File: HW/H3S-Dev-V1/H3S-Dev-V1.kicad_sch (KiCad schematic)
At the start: 74 parts, among them J1 USB_C_Receptacle_USB2.0_16P, J2 Conn_01x02, J3 Conn_Coaxial, J4 Conn_01x04, J5 Conn_01x04, Q1 DMP3099L, SW1 SW_Push, SW2 SW_Push, U1 Ra-01SH-P, U2 LTC4054ES5-4.2, U3 USBLC6-2SC6, U4 ESP32-S3-WROOM-1, U5 SY8089AAAC, U6 L96-M33

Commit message: Routing progress
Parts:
- added C14: 22u, Capacitor_SMD:C_0805_2012Metric_Pad1.18x1.45mm_HandSolder, symbol Device:C
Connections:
- net GND: now also C14.2
- net VCC: now also C14.1
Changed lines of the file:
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@@
 	(wire
 		(pts
+			(xy 372.11 73.66) (xy 372.11 80.01)
+		)
+		(stroke
+			(width 0)
+			(type default)
+		)
+	)
+	(wire
+		(pts
 			(xy 154.94 185.42) (xy 154.94 189.23)
 		)
@@
 	(wire
 		(pts
+			(xy 372.11 92.71) (xy 372.11 87.63)
+		)
+		(stroke
+			(width 0)
+			(type default)
+		)
+	)
+	(wire
+		(pts
 			(xy 57.15 82.55) (xy 40.64 82.55)
 		)
@@
 	)
 	(symbol
+		(lib_id "power:GND")
+		(at 372.11 92.71 0)
+		(unit 1)
+		(exclude_from_sim no)
+		(in_bom yes)
+		(on_board yes)
+		(dnp no)
+		(fields_autoplaced yes)
+		(property "Reference" "#PWR049"
+			(at 372.11 99.06 0)
+			(effects
+				(font
+					(size 1.27 1.27)
+				)
+				(hide yes)
+			)
+		)
+		(property "Value" "GND"
+			(at 372.11 97.79 0)
+			(effects
+				(font
+					(size 1.27 1.27)
+				)
+			)
+		)
+		(property "Footprint" ""
+			(at 372.11 92.71 0)
+			(effects
+				(font
+					(size 1.27 1.27)
+				)
+				(hide yes)
+			)
+		)
+		(property "Datasheet" ""
+			(at 372.11 92.71 0)
+			(effects
+				(font
+					(size 1.27 1.27)
+				)
+				(hide yes)
+			)
+		)
+		(property "Description" "Power symbol creates a global label with name \"GND\" , ground"
+			(at 372.11 92.71 0)
+			(effects
+				(font
+					(size 1.27 1.27)
+				)
+				(hide yes)
+			)
+		)
+		(pin "1"
+		)
+		(instances
+			(project "H3S-Dev-V1"
+				(path "/bea38324-05bc-47f3-9040-a69798280d79"
+					(reference "#PWR049")
+					(unit 1)
+				)
+			)
+		)
+	)
+	(symbol
 		(lib_id "RF_Module:ESP32-S3-WROOM-1")
 		(at 144.78 139.7 0)
@@
 					(unit 1)
 				)
+			)
+		)
+	)
+	(symbol
+		(lib_id "power:VCC")
+		(at 372.11 73.66 0)
+		(unit 1)
+		(exclude_from_sim no)
+		(in_bom yes)
+		(on_board yes)
+		(dnp no)
+		(fields_autoplaced yes)
+		(property "Reference" "#PWR048"
+			(at 372.11 77.47 0)
+			(effects
+				(font
+					(size 1.27 1.27)
+				)
+				(hide yes)
+			)
+		)
+		(property "Value" "VCC"
+			(at 372.11 68.58 0)
+			(effects
+				(font
+					(size 1.27 1.27)
+				)
+			)
+		)
+		(property "Footprint" ""
+			(at 372.11 73.66 0)
+			(effects
+				(font
+					(size 1.27 1.27)
+				)
+				(hide yes)
+			)
+		)
+		(property "Datasheet" ""
+			(at 372.11 73.66 0)
+			(effects
+				(font
+					(size 1.27 1.27)
+				)
+				(hide yes)
+			)
+		)
+		(property "Description" "Power symbol creates a global label with name \"VCC\""
+			(at 372.11 73.66 0)
+			(effects
+				(font
+					(size 1.27 1.27)
+				)
+				(hide yes)
+			)
+		)
+		(pin "1"
+		)
+		(instances
+			(project "H3S-Dev-V1"
+				(path "/bea38324-05bc-47f3-9040-a69798280d79"
+					(reference "#PWR048")
+					(unit 1)
+				)
+			)
+		)
+	)
+	(symbol
+		(lib_id "Device:C")
+		(at 372.11 83.82 0)
+		(unit 1)
+		(exclude_from_sim no)
+		(in_bom yes)
+		(on_board yes)
+		(dnp no)
+		(property "Reference" "C14"
+			(at 368.554 81.28 0)
+			(effects
+				(font
+					(size 1.27 1.27)
+				)
+				(justify left)
+			)
+		)
+		(property "Value" "22u"
+			(at 368.046 86.106 0)
+			(effects
+				(font
+					(size 1.27 1.27)
+				)
+				(justify left)
+			)
+		)
+		(property "Footprint" "Capacitor_SMD:C_0805_2012Metric_Pad1.18x1.45mm_HandSolder"
+			(at 373.0752 87.63 0)
+			(effects
+				(font
+					(size 1.27 1.27)
+				)
+				(hide yes)
+			)
+		)
+		(property "Datasheet" "~"
+			(at 372.11 83.82 0)
+			(effects
+				(font
+					(size 1.27 1.27)
+				)
+				(hide yes)
+			)
+		)
+		(property "Description" "Unpolarized capacitor"
+			(at 372.11 83.82 0)
+			(effects
+				(font
+					(size 1.27 1.27)
+				)
+				(hide yes)
+			)
+		)
+		(pin "1"
+		)
+		(pin "2"
+		)
+		(instances
+			(project "H3S-Dev-V1"
+				(path "/bea38324-05bc-47f3-9040-a69798280d79"
+					(reference "C14")
+					(unit 1)
+				)

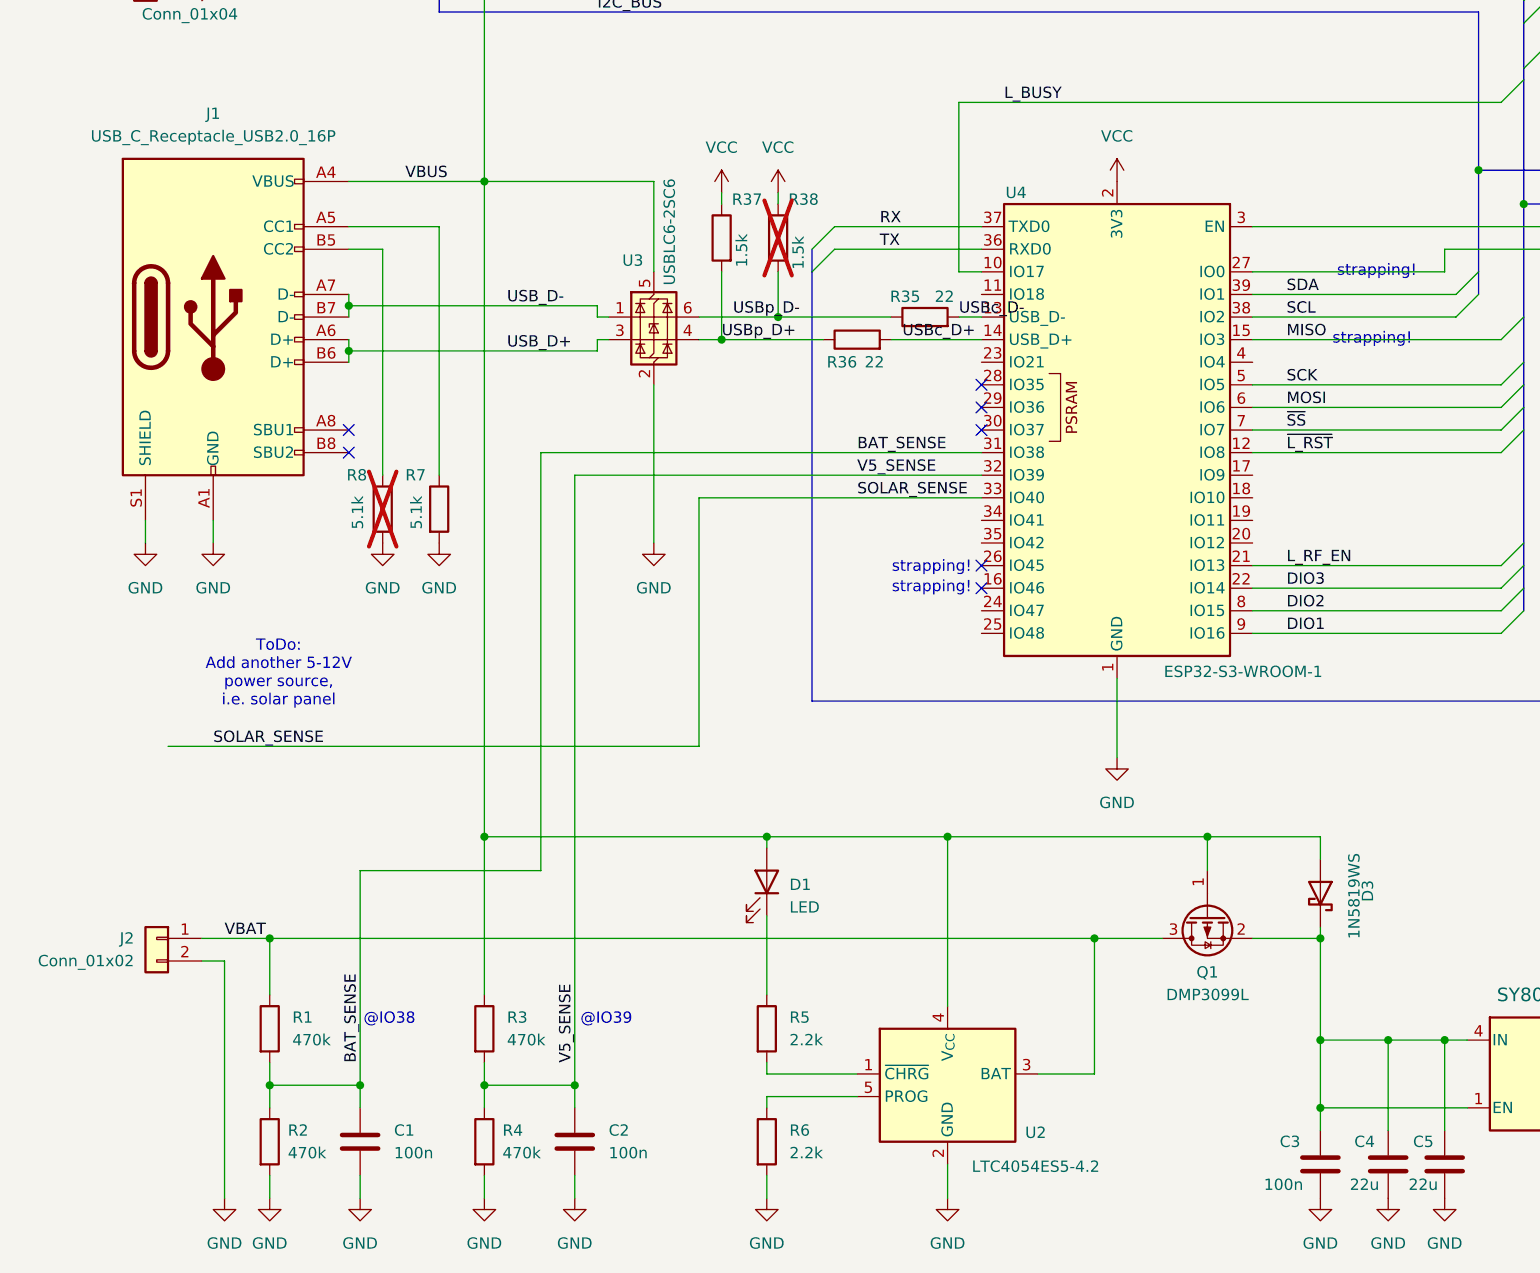
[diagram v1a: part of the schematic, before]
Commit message: Solar connector added
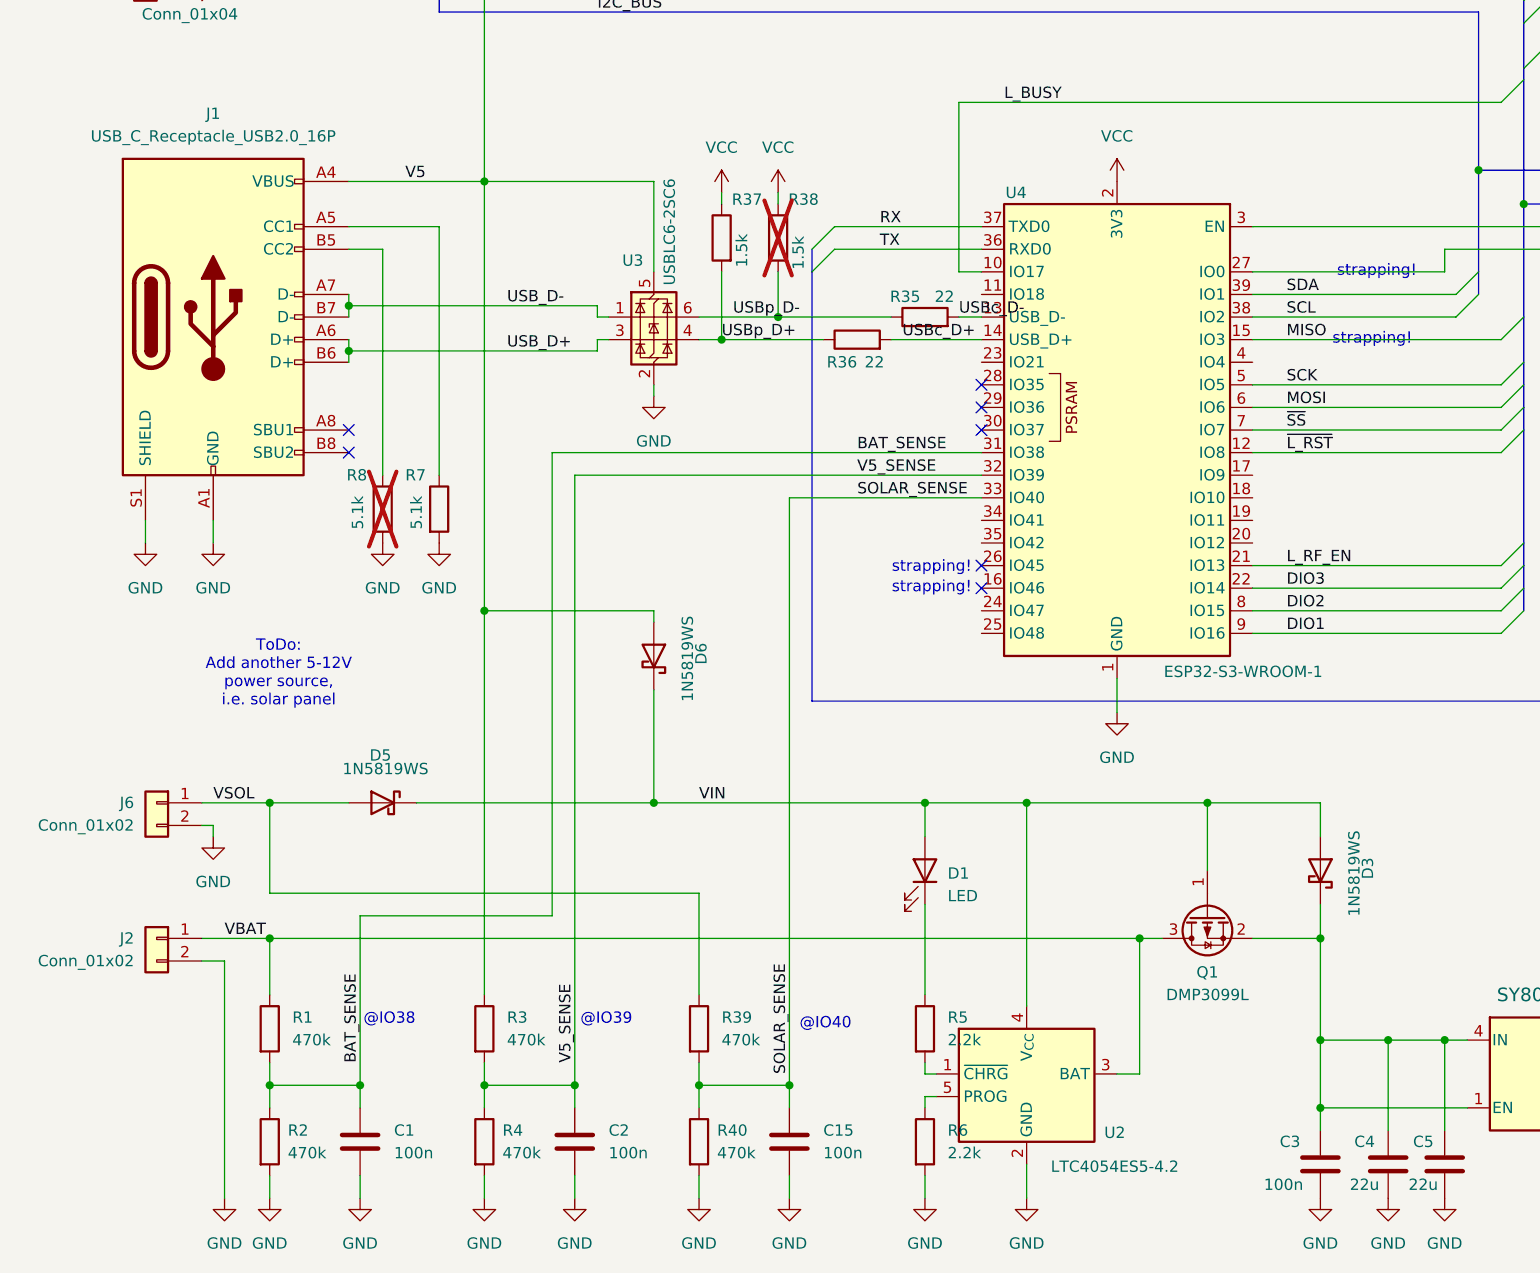
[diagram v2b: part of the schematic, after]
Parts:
- added C15: 100n, Capacitor_SMD:C_0603_1608Metric, symbol Device:C
- added D5, D6: 1N5819WS, Diode_SMD:D_SOD-323, symbol Diode:1N5819WS
- added J6: Conn_01x02, Connector_JST:JST_PH_B2B-PH-K_1x02_P2.00mm_Vertical, symbol Connector_Generic:Conn_01x02
- added R39, R40: 470k, Resistor_SMD:R_0603_1608Metric, symbol Device:R
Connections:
- net GND: now also C15.2, J6.2 (Pin_2), R40.2
- net SOLAR_SENSE: now also C15.1, R39.2, R40.1
- net VBUS renamed V5
- net V5: now also D6.2 (A); no longer D1.2 (A), D3.2 (A), Q1.1 (G), U2.4 (V_{CC})
- new net VIN: D1.2 (A), D3.2 (A), D5.1 (K), D6.1 (K), Q1.1 (G), U2.4 (V_{CC})
- new net VSOL: D5.2 (A), J6.1 (Pin_1), R39.1
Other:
- note added: "@IO40"
- moved on the sheet: D1, D3, R5, R6, U2

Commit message: To review
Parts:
- added TP1: VIN, Connector_PinHeader_1.27mm:PinHeader_1x01_P1.27mm_Vertical, symbol Connector:TestPoint
- J6: footprint Connector_JST:JST_PH_B2B-PH-K_1x02_P2.00mm_Vertical -> Connector_JST:JST_XA_B02B-XASK-1_1x02_P2.50mm_Vertical
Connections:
- net VIN: now also TP1.1
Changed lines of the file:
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@@
 	)
 	(junction
+		(at 167.64 181.61)
+		(diameter 0)
+		(color 0 0 0 0)
+	)
+	(junction
 		(at 57.15 50.8)
 		(diameter 0)
@@
 	)
 	(symbol
+		(lib_id "Connector:TestPoint")
+		(at 167.64 181.61 0)
+		(unit 1)
+		(exclude_from_sim no)
+		(in_bom yes)
+		(on_board yes)
+		(dnp yes)
+		(fields_autoplaced yes)
+		(property "Reference" "TP1"
+			(at 170.18 177.0379 0)
+			(effects
+				(font
+					(size 1.27 1.27)
+				)
+				(justify left)
+			)
+		)
+		(property "Value" "VIN"
+			(at 170.18 179.5779 0)
+			(effects
+				(font
+					(size 1.27 1.27)
+				)
+				(justify left)
+			)
+		)
+		(property "Footprint" "Connector_PinHeader_1.27mm:PinHeader_1x01_P1.27mm_Vertical"
+			(at 172.72 181.61 0)
+			(effects
+				(font
+					(size 1.27 1.27)
+				)
+				(hide yes)
+			)
+		)
+		(property "Datasheet" "~"
+			(at 172.72 181.61 0)
+			(effects
+				(font
+					(size 1.27 1.27)
+				)
+				(hide yes)
+			)
+		)
+		(property "Description" "test point"
+			(at 167.64 181.61 0)
+			(effects
+				(font
+					(size 1.27 1.27)
+				)
+				(hide yes)
+			)
+		)
+		(pin "1"
+		)
+		(instances
+			(project ""
+				(path "/bea38324-05bc-47f3-9040-a69798280d79"
+					(reference "TP1")
+					(unit 1)
+				)
+			)
+		)
+	)
+	(symbol
 		(lib_id "power:VCC")
 		(at 243.84 208.28 270)
@@
 			)
 		)
-		(property "Footprint" "Connector_JST:JST_PH_B2B-PH-K_1x02_P2.00mm_Vertical"
+		(property "Footprint" "Connector_JST:JST_XA_B02B-XASK-1_1x02_P2.50mm_Vertical"
 			(at 36.83 181.61 0)
 			(effects

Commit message: BOM Preparation
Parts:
- C1, C10, C11, C12, C13, C14, C15, C2, C3, C4, C5, C6, C7, C8, C9, D1, D2, D4, R1, R10, R11, R12, R13, R14, R15, R16, R17, R18, R19, R2, R20, R21, R22, R23, R24, R25, R26, R27, R28, R29, R3, R30, R31, R32, R33, R34, R35, R36, R37, R38, R39, R4, R40, R5, R6, R7, R8, R9: Type (none) -> SMD
- D3, D5, D6: P/N (none) -> 1N5819HW1-7-F; Type (none) -> SMD
- J1: Type (none) -> Mixed
- J2, J4, J5, J6: Type (none) -> THT
- J3: P/N (none) -> U.FL-R-SMT-1(10); Type (none) -> SMD
- L1: P/N (none) -> LCSCPN C136245; Type (none) -> SMD
- Q1: P/N (none) -> DMP3099L-7 / WPM2015-3; Type (none) -> SMD
- SW1, SW2: P/N (none) -> PTS636SK25SMTRLFS; Type (none) -> SMD
- TP1: now left out of the parts list
- U1: MF (none) -> Ai-Thinker; P/N (none) -> Ra-01SH-P; Type (none) -> SMD
- U2: MF (none) -> LT; P/N (none) -> BL4054B; Type (none) -> SMD
- U3: P/N (none) -> USBLC6-2SC6; Type (none) -> SMD
- U4: MF (none) -> Espressif; P/N (none) -> ESP32-S3-WROOM-1U-N16R8; Type (none) -> SMD
- U5: MF (none) -> Silergy; P/N (none) -> SY8089AAAC; Type (none) -> SMD
- U6: MF Quectel Wireless Solutions Co., Ltd -> Quectel; P/N (none) -> L96-M33; Type (none) -> SMD

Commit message: PCB updates
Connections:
- net 3D: now also U4.18 (IO10)
- net FO: now also U4.11 (IO18)
- net GF: now also U4.20 (IO12)
- net INT: now also U4.4 (IO4)
- net JD: now also U4.19 (IO11)
- net TP: now also U4.17 (IO9)

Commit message: PCB updates
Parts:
- added D7: LED, LED_SMD:LED_0603_1608Metric, symbol Device:LED
- added R41: 10k, Resistor_SMD:R_0603_1608Metric, symbol Device:R
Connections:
- net GND: now also R41.2
- net INT: now also U4.23 (IO21); no longer U4.4 (IO4)
- new net: D7.1 (K), R41.1
- new net LED: D7.2 (A), U4.4 (IO4)
